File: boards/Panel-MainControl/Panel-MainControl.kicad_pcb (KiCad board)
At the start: 2 copper layers, 142.1 x 72.1 mm, 26 parts, among them J1 ISP, J10 Conn_01x10, J11 Conn_01x10, J2 PanelRight, J3 Volume, J4 Btn1, J5 Btn3, J6 Btn5, J7 Btn2, J8 Btn4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

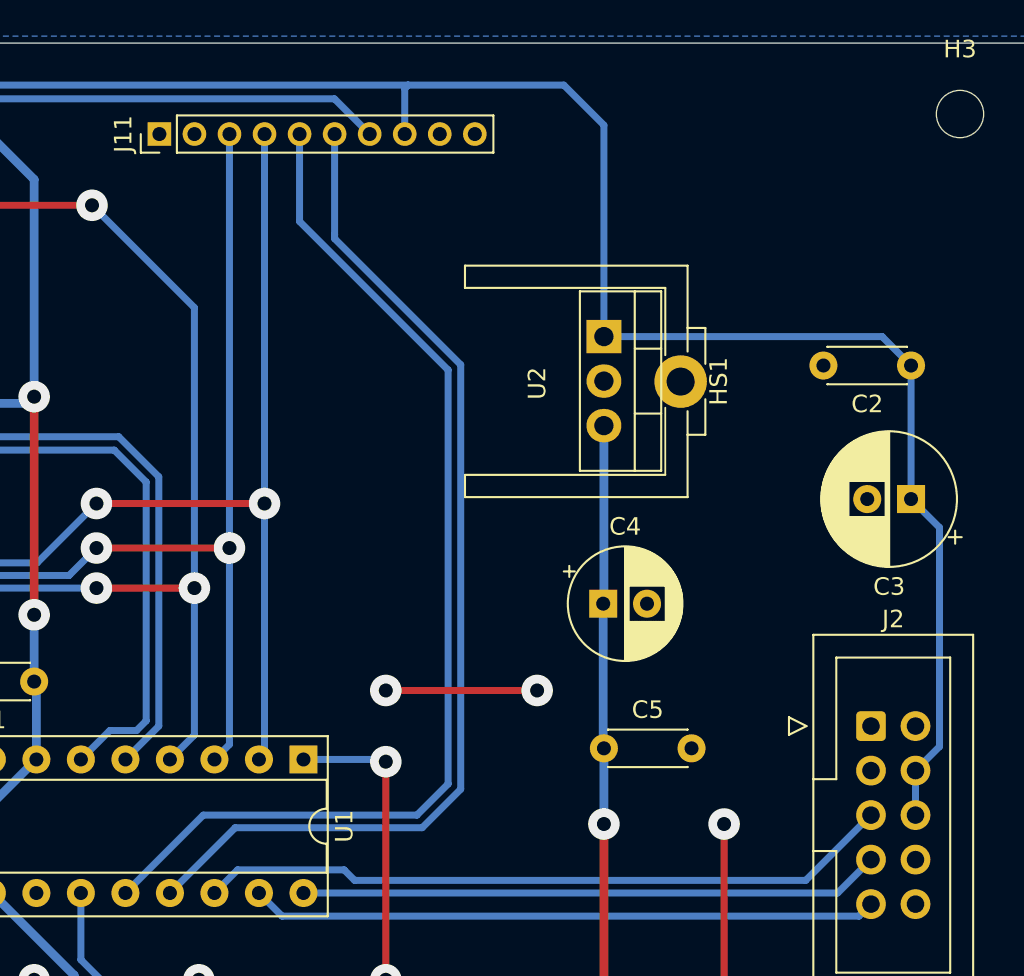
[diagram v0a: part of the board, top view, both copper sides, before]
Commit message: Fixed using 5V from main power for PWR LED
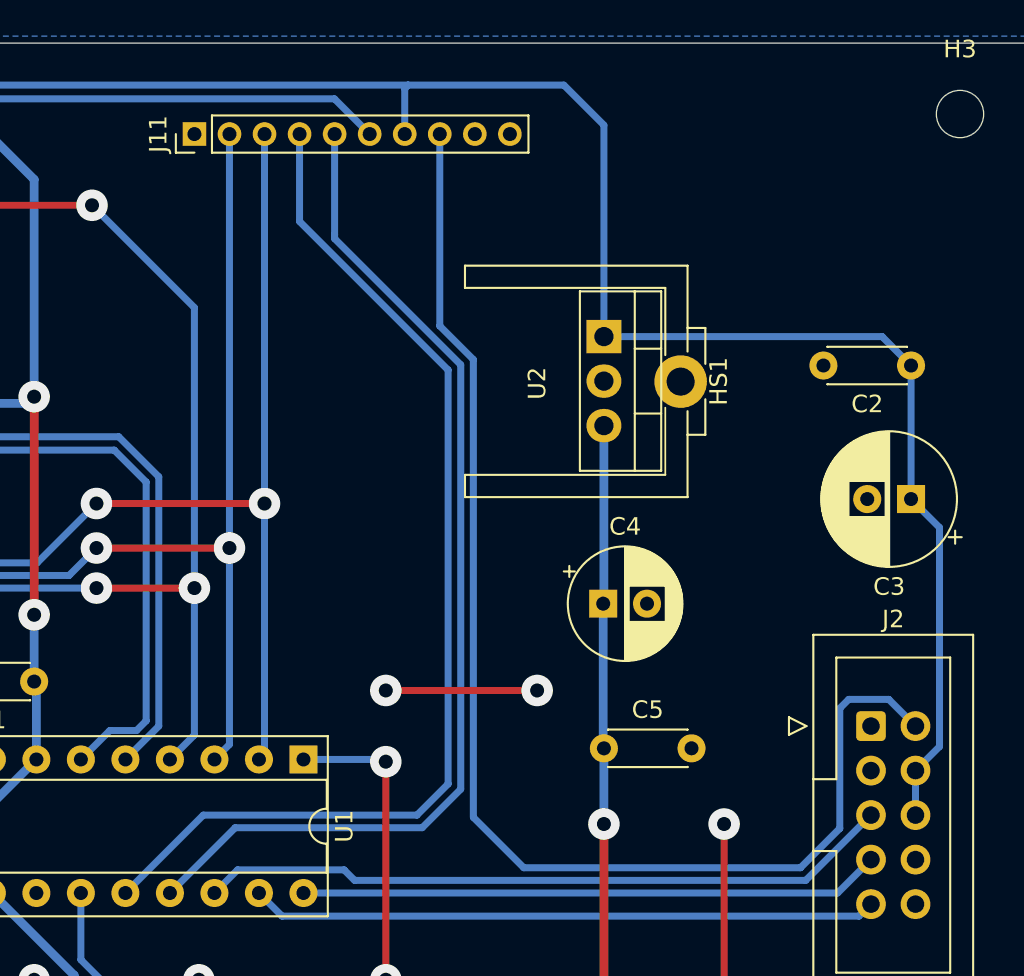
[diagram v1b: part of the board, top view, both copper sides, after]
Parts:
- moved J11 2.00 mm to (190.0, 61.5)
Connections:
- J11 pad 2: unconnected-(J11-Pin_2-Pad2) -> /KP_Line2
- J11 pad 3: /KP_Line2 -> /KP_Line3
- J11 pad 4: /KP_Line3 -> /FX2
- J11 pad 5: /FX2 -> /FX1
- J11 pad 6: /FX1 -> /LED_Ctrl
- J11 pad 7: /LED_Ctrl -> +12V
- J11 pad 8: +12V -> +5VA
- J2 pad 2: unconnected-(J2-Pin_2-Pad2) -> +5VA
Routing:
- net +5VA: track 0.00 -> 74.8 mm
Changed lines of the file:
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@@
 	(net 8 "/MOSI")
 	(net 9 "unconnected-(J1-Pin_3-Pad3)")
-	(net 10 "unconnected-(J2-Pin_2-Pad2)")
+	(net 10 "+5VA")
 	(net 11 "unconnected-(J2-Pin_3-Pad3)")
 	(net 12 "unconnected-(J2-Pin_1-Pad1)")
@@
 	(net 49 "unconnected-(U4-~{Z}-Pad6)")
 	(net 50 "unconnected-(J11-Pin_1-Pad1)")
-	(net 51 "unconnected-(J11-Pin_2-Pad2)")
 	(footprint "Connector_PinHeader_2.54mm:PinHeader_1x03_P2.54mm_Vertical"
 		(layer "F.Cu")
@@
 		(tags "Through hole pin header THT 1x03 2.54mm single row")
 		(property "Reference" "J3"
-			(at 0 -2.33 360)
+			(at 0 -2.33 0)
 			(layer "F.SilkS")
 			(effects
@@
 		)
 		(property "Value" "Volume"
-			(at 0 7.41 360)
+			(at 0 7.41 0)
 			(layer "F.Fab")
 			(effects
@@
 		(tags "C Disc series Radial pin pitch 5.00mm  diameter 4.3mm width 1.9mm Capacitor")
 		(property "Reference" "C5"
-			(at 2.5 -2.2 360)
+			(at 2.5 -2.2 0)
 			(layer "F.SilkS")
 			(effects
@@
 		)
 		(property "Value" "100nF"
-			(at 2.5 2.2 360)
+			(at 2.5 2.2 0)
 			(layer "F.Fab")
 			(effects
@@
 		)
 		(fp_text user "${REFERENCE}"
-			(at 2.5 0 360)
+			(at 2.5 0 0)
 			(layer "F.Fab")
 			(effects
@@
 		(tags "CP Radial series Radial pin pitch 2.50mm  diameter 7.5mm Electrolytic Capacitor")
 		(property "Reference" "C3"
-			(at 1.25 -5 360)
+			(at 1.25 -5 0)
 			(layer "F.SilkS")
 			(effects
@@
 		)
 		(property "Value" "33uF"
-			(at 1.25 5 360)
+			(at 1.25 5 0)
 			(layer "F.Fab")
 			(effects
@@
 		)
 		(fp_text user "${REFERENCE}"
-			(at 1.25 0 360)
+			(at 1.25 0 0)
 			(layer "F.Fab")
 			(effects
@@
 	(footprint "Connector_PinHeader_2.00mm:PinHeader_1x10_P2.00mm_Vertical"
 		(layer "F.Cu")
-		(at 187.994 61.468 90)
+		(at 189.994 61.468 90)
 		(descr "Through hole straight pin header, 1x10, 2.00mm pitch, single row")
 		(tags "Through hole pin header THT 1x10 2.00mm single row")
@@
 			(layers "*.Cu" "*.Mask")
 			(remove_unused_layers no)
-			(net 51 "unconnected-(J11-Pin_2-Pad2)")
+			(net 20 "/KP_Line2")
 			(pinfunction "Pin_2")
-			(pintype "passive+no_connect")
+			(pintype "passive")
 		)
 		(pad "3" thru_hole oval
@@
 			(layers "*.Cu" "*.Mask")
 			(remove_unused_layers no)
-			(net 20 "/KP_Line2")
+			(net 23 "/KP_Line3")
 			(pinfunction "Pin_3")
 			(pintype "passive")
@@
 			(layers "*.Cu" "*.Mask")
 			(remove_unused_layers no)
-			(net 23 "/KP_Line3")
+			(net 29 "/FX2")
 			(pinfunction "Pin_4")
 			(pintype "passive")
@@
 			(layers "*.Cu" "*.Mask")
 			(remove_unused_layers no)
-			(net 29 "/FX2")
+			(net 33 "/FX1")
 			(pinfunction "Pin_5")
 			(pintype "passive")
@@
 			(layers "*.Cu" "*.Mask")
 			(remove_unused_layers no)
-			(net 33 "/FX1")
+			(net 37 "/LED_Ctrl")
 			(pinfunction "Pin_6")
 			(pintype "passive")
@@
 			(layers "*.Cu" "*.Mask")
 			(remove_unused_layers no)
-			(net 37 "/LED_Ctrl")
+			(net 3 "+12V")
 			(pinfunction "Pin_7")
 			(pintype "passive")
@@
 			(layers "*.Cu" "*.Mask")
 			(remove_unused_layers no)
-			(net 3 "+12V")
+			(net 10 "+5VA")
 			(pinfunction "Pin_8")
 			(pintype "passive")
@@
 		(tags "C Disc series Radial pin pitch 5.00mm  diameter 4.3mm width 1.9mm Capacitor")
 		(property "Reference" "C1"
-			(at 2.5 -2.2 360)
+			(at 2.5 -2.2 0)
 			(layer "F.SilkS")
 			(effects
@@
 		)
 		(property "Value" "100nF"
-			(at 2.5 2.2 360)
+			(at 2.5 2.2 0)
 			(layer "F.Fab")
 			(effects
@@
 		)
 		(fp_text user "${REFERENCE}"
-			(at 2.5 0 360)
+			(at 2.5 0 0)
 			(layer "F.Fab")
 			(effects
@@
 		(tags "CP Radial series Radial pin pitch 2.50mm  diameter 6.3mm Electrolytic Capacitor")
 		(property "Reference" "C4"
-			(at 1.25 -4.4 360)
+			(at 1.25 -4.4 0)
 			(layer "F.SilkS")
 			(effects
@@
 		)
 		(property "Value" "10uF"
-			(at 1.25 4.4 360)
+			(at 1.25 4.4 0)
 			(layer "F.Fab")
 			(effects
@@
 		)
 		(fp_text user "${REFERENCE}"
-			(at 1.25 0 360)
+			(at 1.25 0 0)
 			(layer "F.Fab")
 			(effects
@@
 		(tags "THT DIP DIL PDIP 2.54mm 7.62mm 300mil")
 		(property "Reference" "U3"
-			(at 3.81 -2.33 360)
+			(at 3.81 -2.33 0)
 			(layer "F.SilkS")
 			(effects
@@
 		)
 		(property "Value" "ULN2803A"
-			(at 3.81 22.65 360)
+			(at 3.81 22.65 0)
 			(layer "F.Fab")
 			(effects
@@
 		)
 		(fp_text user "${REFERENCE}"
-			(at 3.81 10.16 360)
+			(at 3.81 10.16 0)
 			(layer "F.Fab")
 			(effects
@@
 			(layers "*.Cu" "*.Mask")
 			(remove_unused_layers no)
-			(net 10 "unconnected-(J2-Pin_2-Pad2)")
+			(net 10 "+5VA")
 			(pinfunction "Pin_2")
-			(pintype "passive+no_connect")
+			(pintype "passive")
 		)
 		(pad "3" thru_hole circle
@@
 		(tags "C Disc series Radial pin pitch 5.00mm  diameter 4.3mm width 1.9mm Capacitor")
 		(property "Reference" "C2"
-			(at 2.5 -2.2 360)
+			(at 2.5 -2.2 0)
 			(layer "F.SilkS")
 			(effects
@@
 		)
 		(property "Value" "330nF"
-			(at 2.5 2.2 360)
+			(at 2.5 2.2 0)
 			(layer "F.Fab")
 			(effects
@@
 		)
 		(fp_text user "${REFERENCE}"
-			(at 2.5 0 360)
+			(at 2.5 0 0)
 			(layer "F.Fab")
 			(effects
@@
 		)
 		(fp_text user "${REFERENCE}"
-			(at 1.27 5.08 360)
+			(at 1.27 5.08 0)
 			(layer "F.Fab")
 			(effects
@@
 		(layer "Cmts.User")
 		(pts
-			(xy 233.68 60.325) (xy 205.994 61.468)
+			(xy 233.68 60.325) (xy 208.026 61.468)
 		)
 		(height -8.001)
 		(orientation 0)
-		(gr_text "27,6860 mm"
-			(at 219.837 51.174 0)
+		(gr_text "25,6540 mm"
+			(at 220.853 51.174 0)
 			(layer "Cmts.User")
 			(effects
@@
 		(layer "Cmts.User")
 		(pts
-			(xy 187.994 61.468) (xy 176.53 61.468)
+			(xy 189.994 61.468) (xy 176.53 61.468)
 		)
 		(height -9.652)
 		(orientation 0)
-		(gr_text "11,4640 mm"
-			(at 182.262 50.666 0)
+		(gr_text "13,4640 mm"
+			(at 183.262 50.666 0)
 			(layer "Cmts.User")
 			(effects
@@
 	)
 	(segment
+		(start 229.616 93.726)
+		(end 227.33 93.726)
+		(width 0.4)
+		(layer "B.Cu")
+		(net 10)
+	)
+	(segment
+		(start 205.91 100.457)
+		(end 205.91 74.333532)
+		(width 0.4)
+		(layer "B.Cu")
+		(net 10)
+	)
+	(segment
+		(start 226.820883 101.090883)
+		(end 224.576766 103.335)
+		(width 0.4)
+		(layer "B.Cu")
+		(net 10)
+	)
+	(segment
+		(start 203.994 72.417532)
+		(end 203.994 61.468)
+		(width 0.4)
+		(layer "B.Cu")
+		(net 10)
+	)
+	(segment
+		(start 205.91 74.333532)
+		(end 203.994 72.417532)
+		(width 0.4)
+		(layer "B.Cu")
+		(net 10)
+	)
+	(segment
+		(start 224.576766 103.335)
+		(end 208.788 103.335)
+		(width 0.4)
+		(layer "B.Cu")
+		(net 10)
+	)
+	(segment
+		(start 208.788 103.335)
+		(end 205.91 100.457)
+		(width 0.4)
+		(layer "B.Cu")
+		(net 10)
+	)
+	(segment
+		(start 227.33 93.726)
+		(end 226.820883 94.235117)
+		(width 0.4)
+		(layer "B.Cu")
+		(net 10)
+	)
+	(segment
+		(start 226.820883 94.235117)
+		(end 226.820883 101.090883)
+		(width 0.4)
+		(layer "B.Cu")
+		(net 10)
+	)
+	(segment
+		(start 231.14 95.25)
+		(end 229.616 93.726)
+		(width 0.4)
+		(layer "B.Cu")
+		(net 10)
+	)
+	(segment

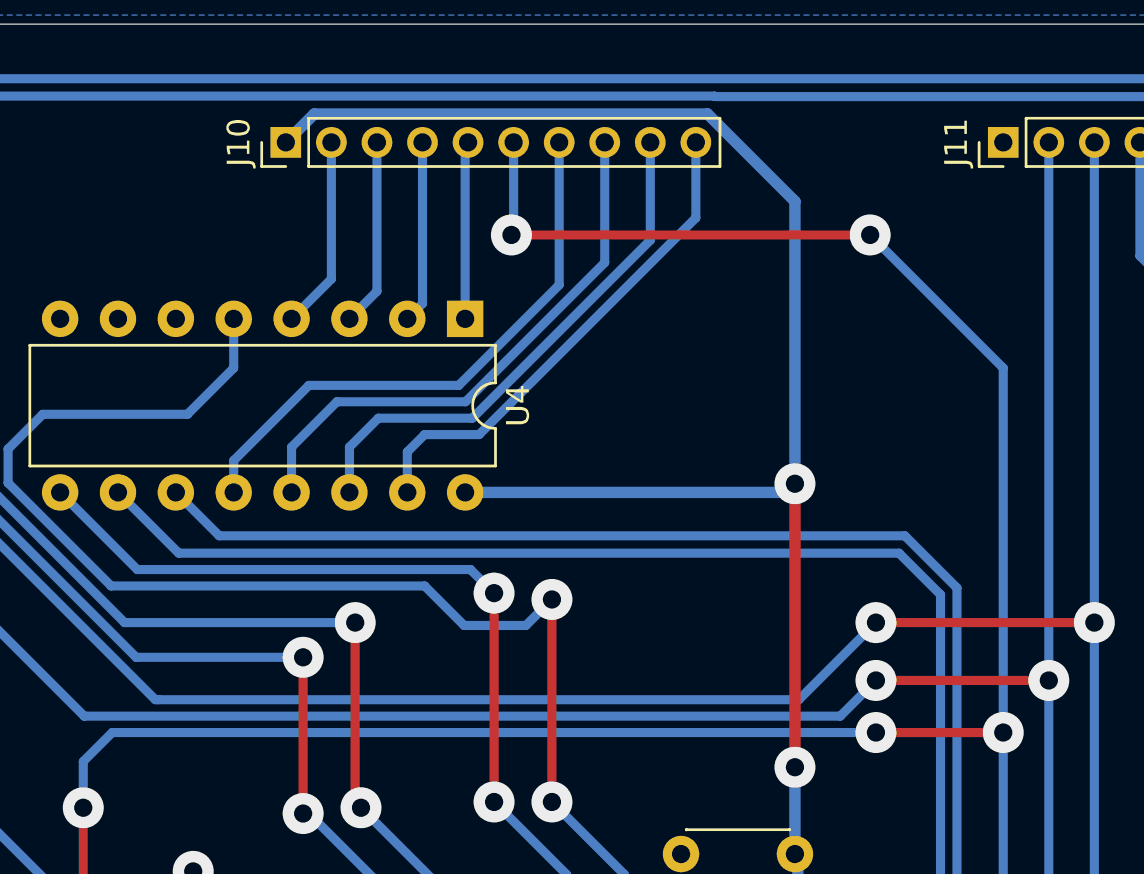
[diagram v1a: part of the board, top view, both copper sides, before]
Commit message: Fixes for missing pullups on keypad buttons
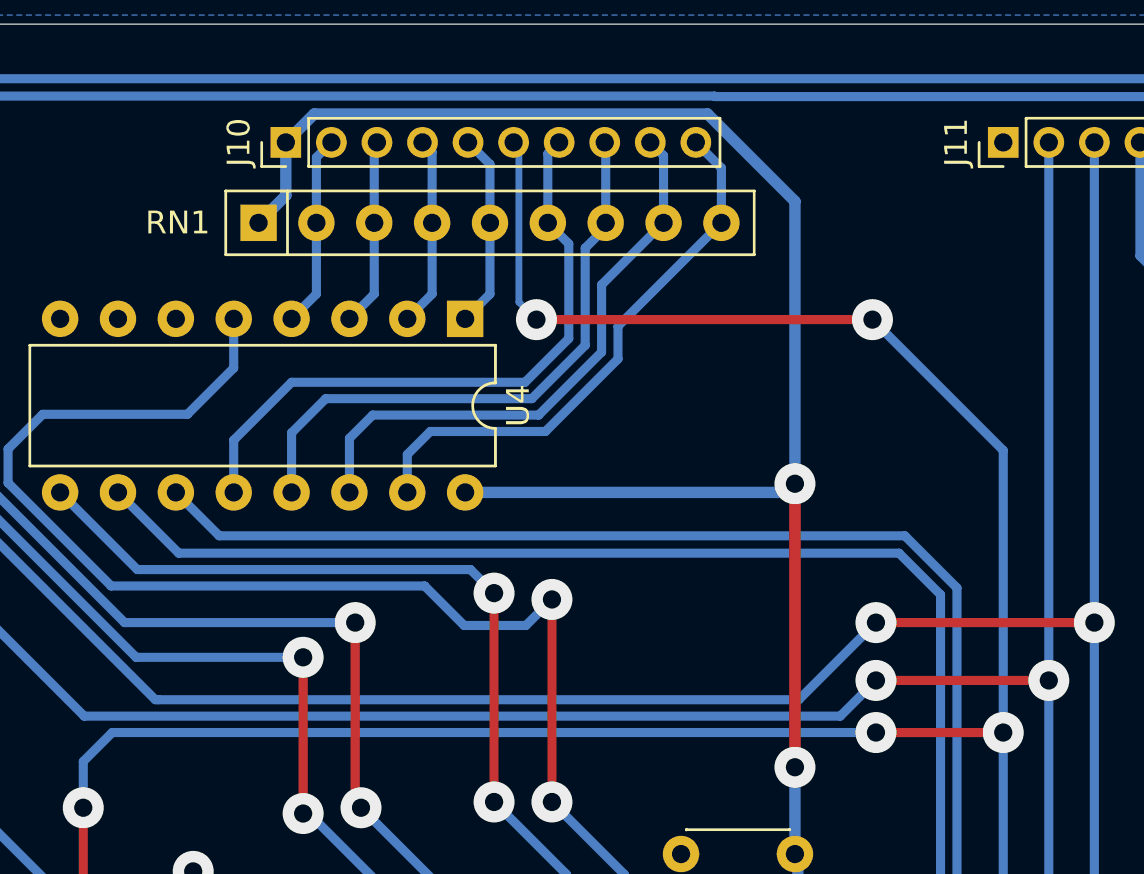
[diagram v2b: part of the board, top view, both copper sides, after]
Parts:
- added RN1: 10k, Resistor_THT:R_Array_SIP9, F.Cu at (157.3, 65.0)
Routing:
- net +5V: track 174.9 -> 178.9 mm
- net /B1: track 25.1 -> 28.1 mm
- net /B2: track 22.0 -> 24.5 mm
- net /A2: track 23.3 -> 25.6 mm
- net /A1: track 24.4 -> 26.4 mm
- net /KP_Col4: track 7.62 -> 8.60 mm
- net /KP_Line1: track 163.2 -> 162.6 mm
